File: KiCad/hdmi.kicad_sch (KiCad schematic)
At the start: 29 parts, among them J22 HDMI_A, Q1 Q_NMOS_GSD, Q2 Q_NMOS_GSD, Q3 Q_NMOS_GSD

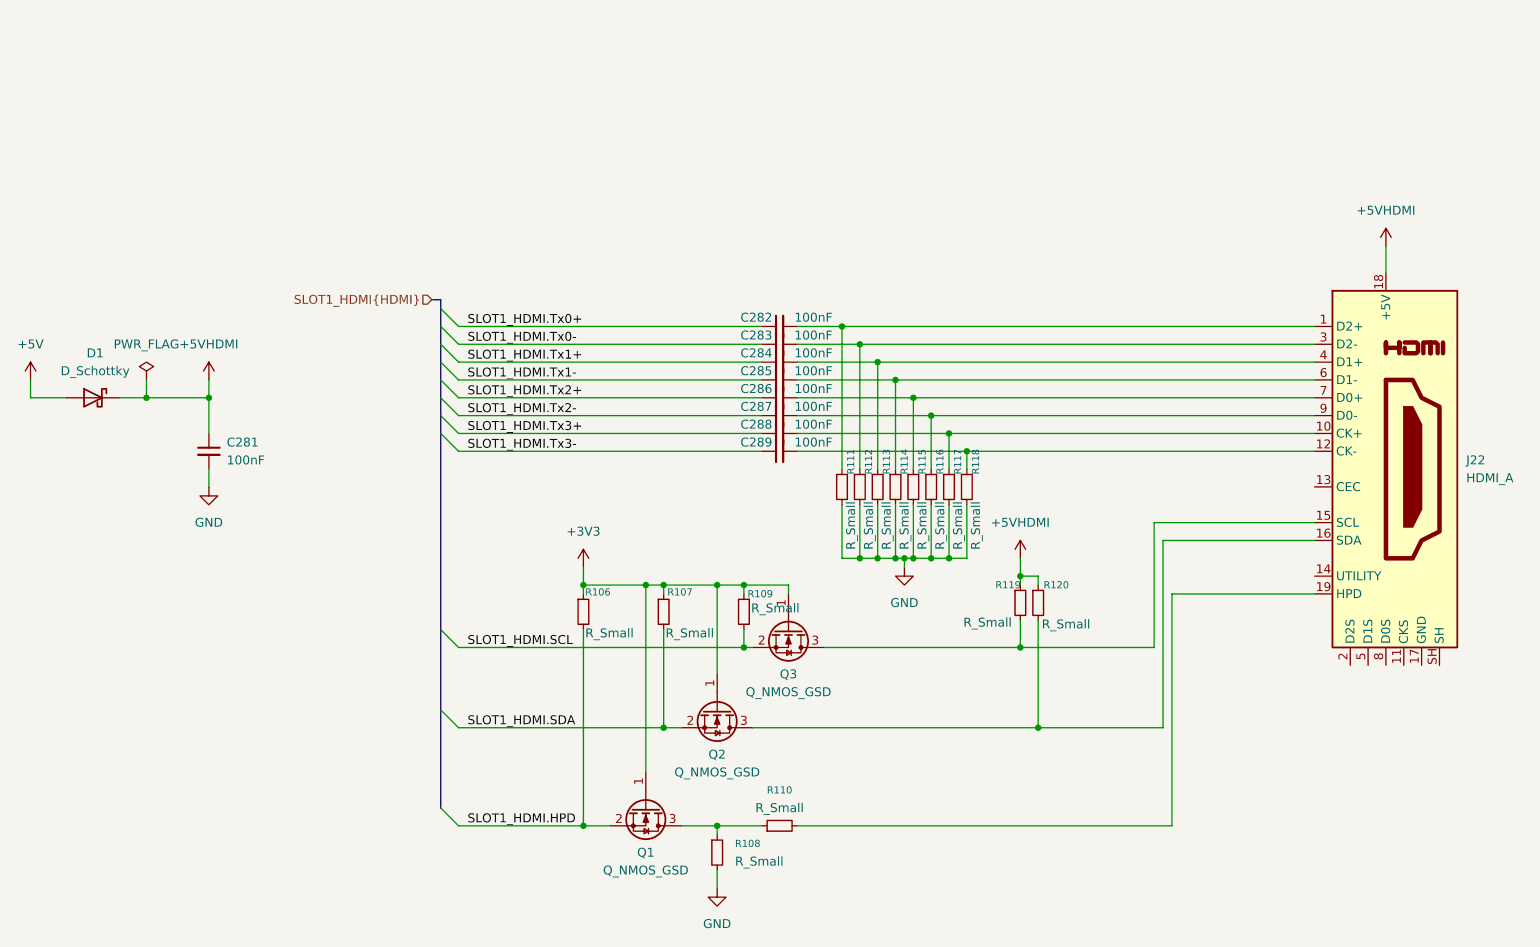
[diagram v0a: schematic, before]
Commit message: Add TPS65987D PD controller, switch stm32 to cheaper one
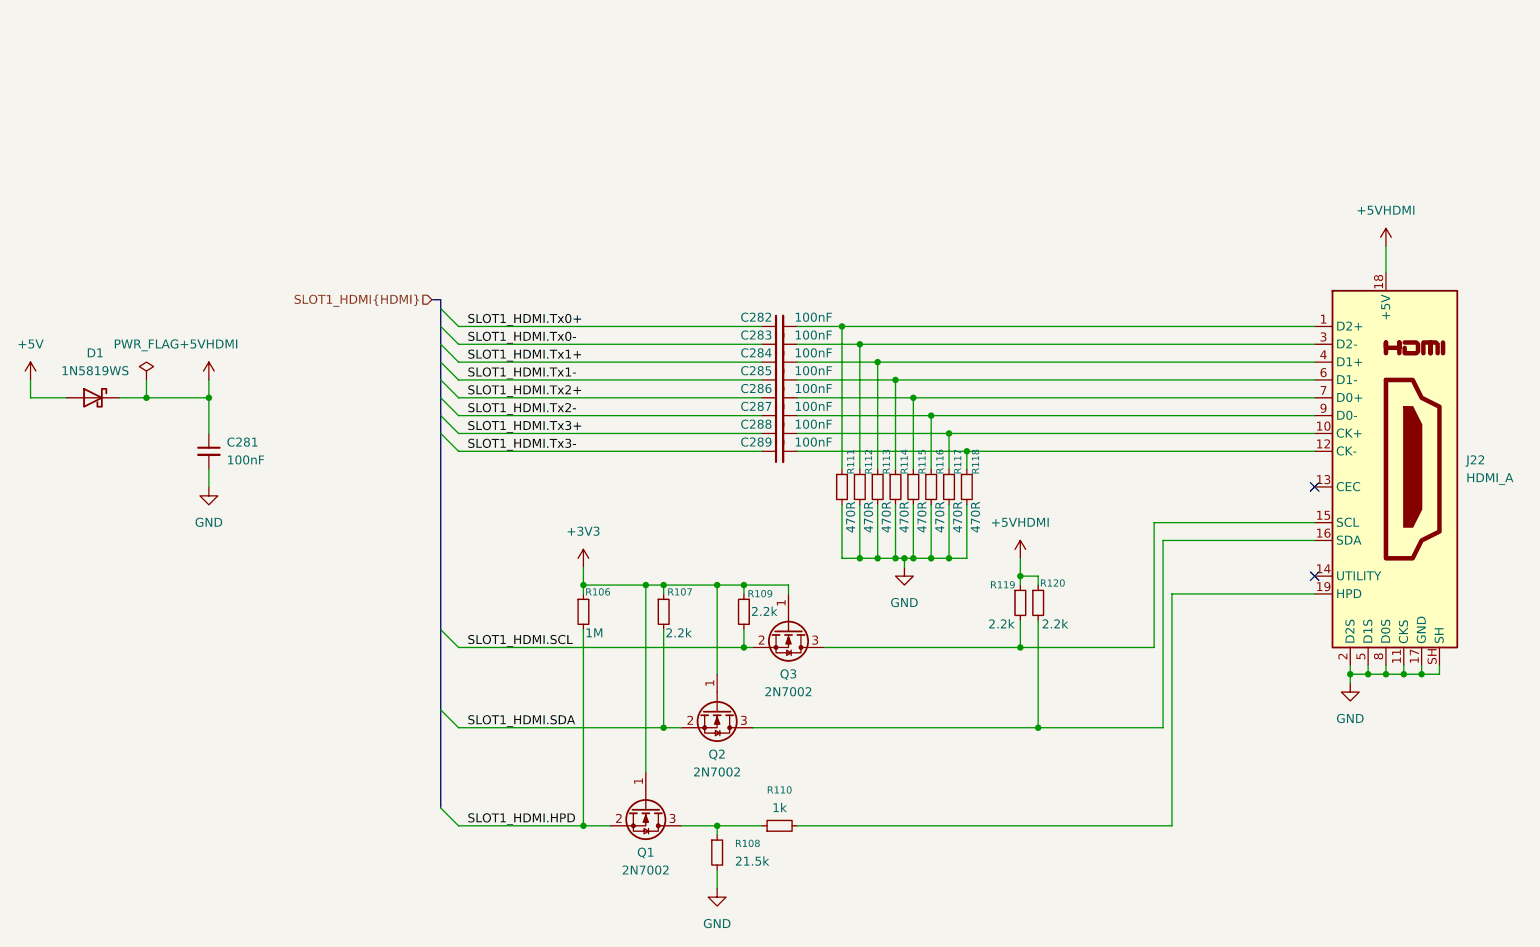
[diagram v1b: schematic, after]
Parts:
- D1: value D_Schottky -> 1N5819WS
- Q1, Q2, Q3: value Q_NMOS_GSD -> 2N7002
- R106: value R_Small -> 1M
- R107, R109, R119, R120: value R_Small -> 2.2k
- R108: value R_Small -> 21.5k
- R110: value R_Small -> 1k
- R111, R112, R113, R114, R115, R116, R117, R118: value R_Small -> 470R
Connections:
- net GND: now also J22.11 (CKS), J22.17 (GND), J22.2 (D2S), J22.5 (D1S), J22.8 (D0S), J22.SH
- no-connect marks 0 -> 2

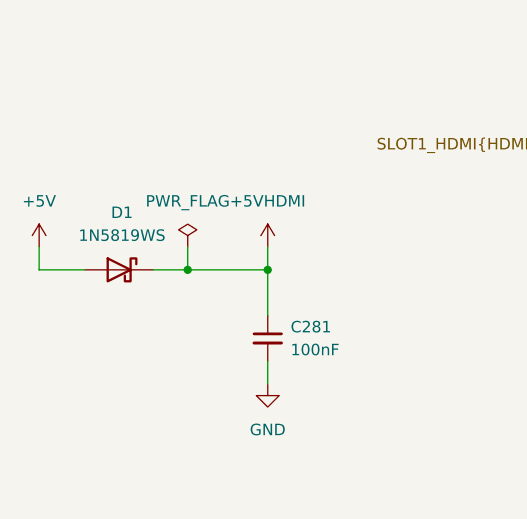
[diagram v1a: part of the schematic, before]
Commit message: Fix some diodes and resistors
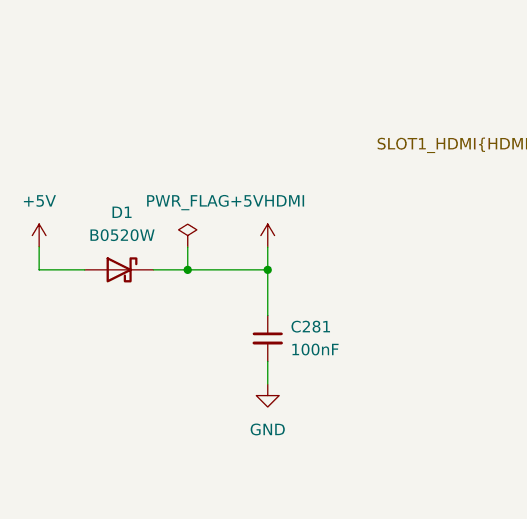
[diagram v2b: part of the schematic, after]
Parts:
- D1: value 1N5819WS -> B0520W
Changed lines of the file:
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@@
 			)
 		)
-		(property "Value" "1N5819WS"
+		(property "Value" "B0520W"
 			(at 46.0375 86.36 0)
 			(effects

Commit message: Re-annotate components
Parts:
- renumbered C281 to C323, C282 to C324, C283 to C325, C284 to C326, C285 to C327, C286 to C328, C287 to C329, C288 to C330, C289 to C331, D1 to D33, J22 to J25, R106 to R202, R107 to R203, R108 to R204, R109 to R205, R110 to R206, R111 to R207, R112 to R208, R113 to R209, R114 to R210, R115 to R211, R116 to R212, R117 to R213, R118 to R214, R119 to R215, R120 to R216

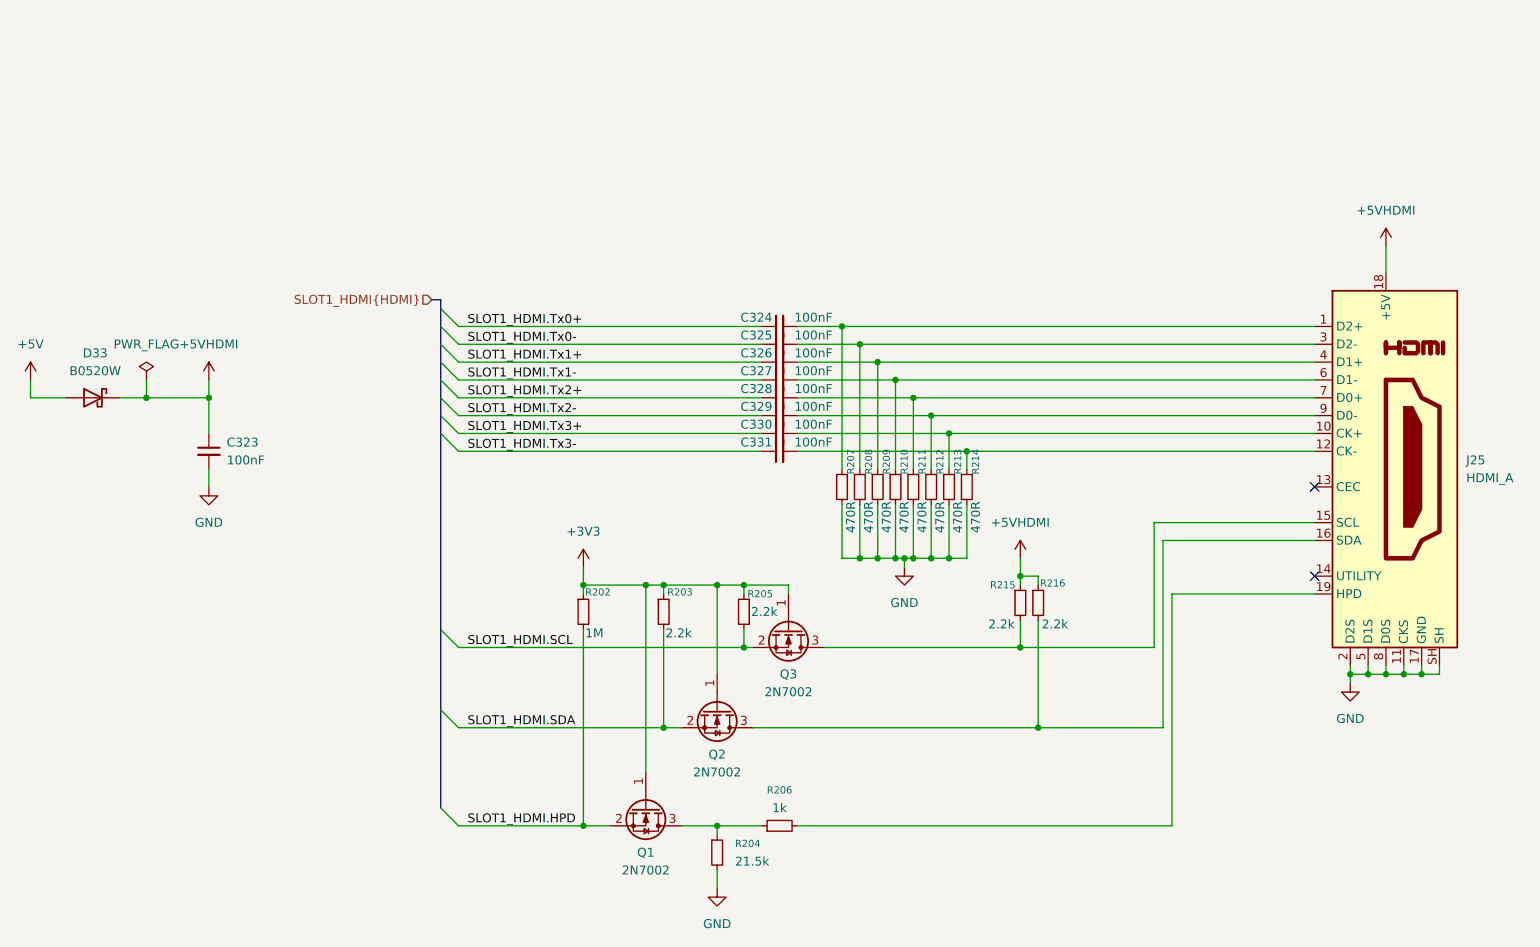
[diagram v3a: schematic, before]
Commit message: Add TVS diodes for ESD protection
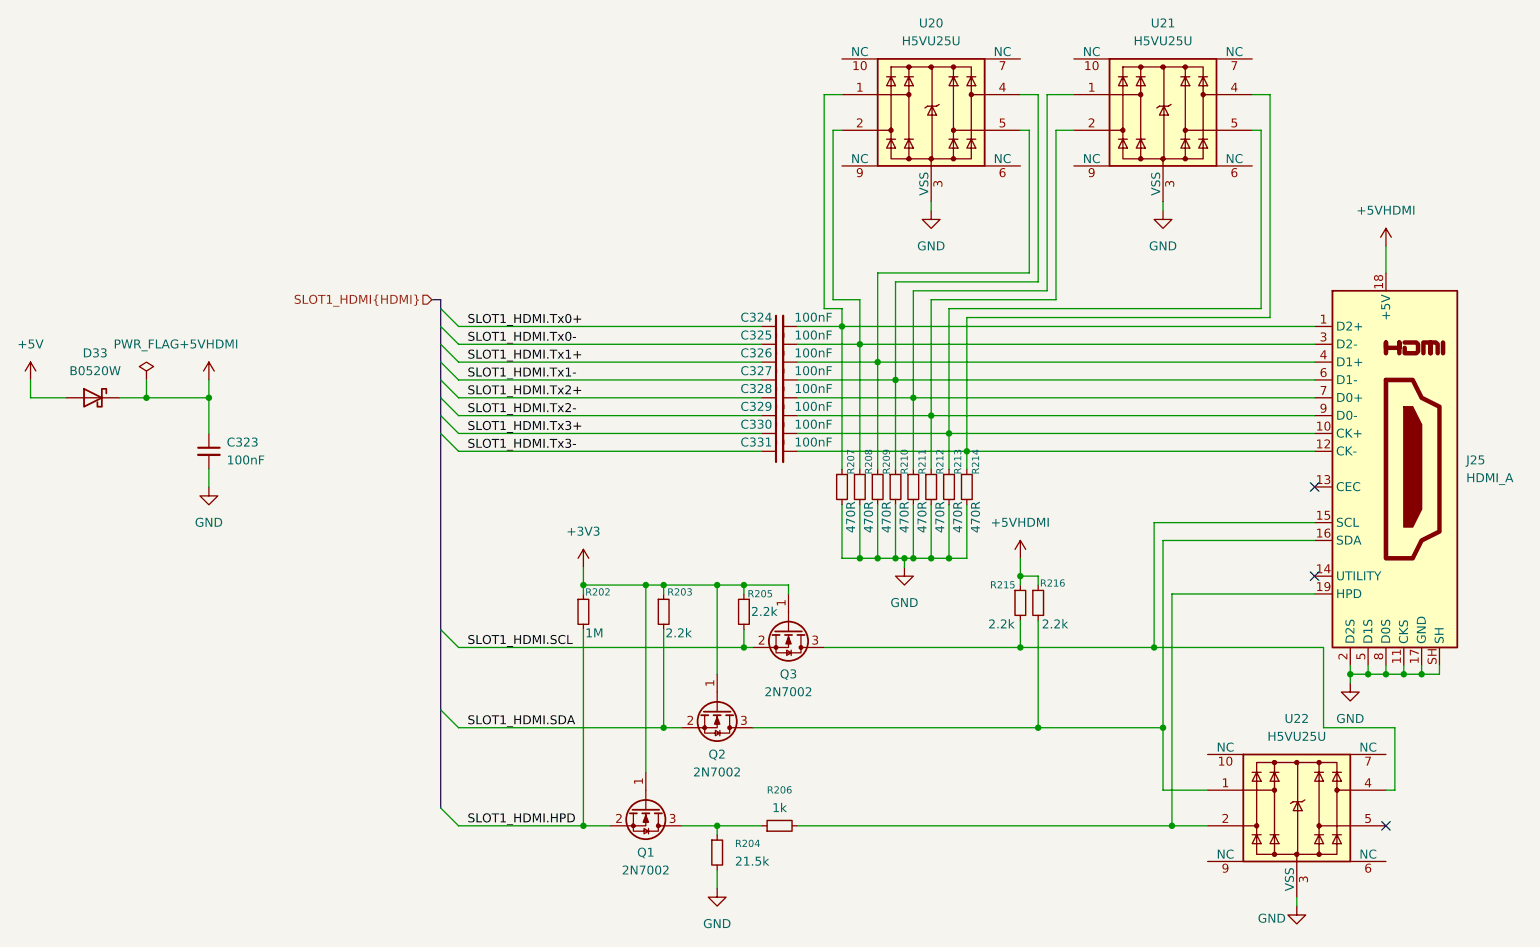
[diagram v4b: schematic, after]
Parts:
- added U20, U21, U22: H5VU25U, Package_DFN_QFN:Diodes_UDFN-10_1.0x2.5mm_P0.5mm, symbol Power_Protection:D3V3XA4B10LP
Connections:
- net GND: now also U20.3 (VSS), U20.8 (VSS), U21.3 (VSS), U21.8 (VSS), U22.3 (VSS), U22.8 (VSS)
- net at C327.2, J25.6 (D1-), R210.1: now also U20.4
- net at J25.16 (SDA), Q2.3 (D), R216.2: now also U22.1
- net at J25.19 (HPD), R206.2: now also U22.2
- net at C326.2, J25.4 (D1+), R209.1: now also U20.5
- net at C324.2, J25.1 (D2+), R207.1: now also U20.1
- net at C330.2, J25.10 (CK+), R213.1: now also U21.5
- net at C331.2, J25.12 (CK-), R214.1: now also U21.4
- net at J25.15 (SCL), Q3.3 (D), R215.2: now also U22.4
- net at C325.2, J25.3 (D2-), R208.1: now also U20.2
- net at C328.2, J25.7 (D0+), R211.1: now also U21.1
- net at C329.2, J25.9 (D0-), R212.1: now also U21.2
- no-connect marks 2 -> 3
